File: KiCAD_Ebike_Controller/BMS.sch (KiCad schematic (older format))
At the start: 3 parts

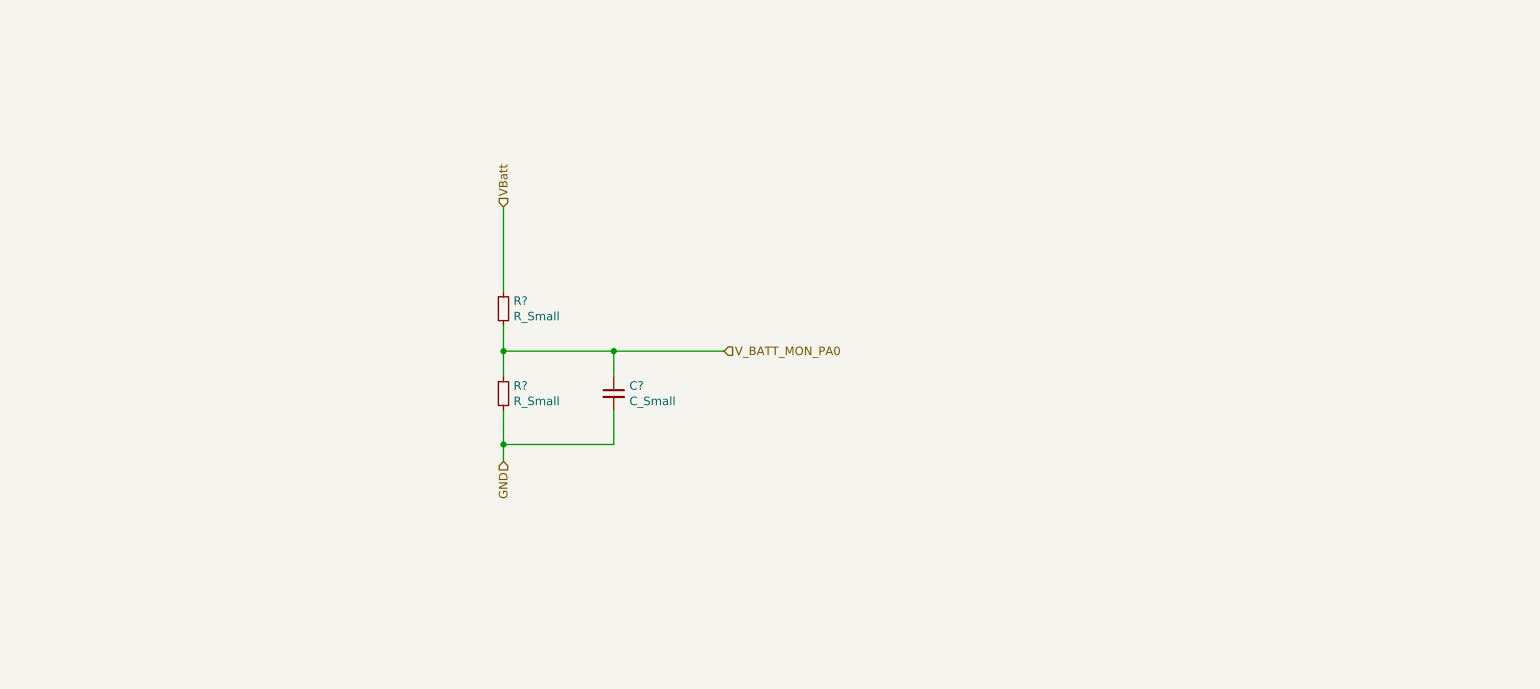
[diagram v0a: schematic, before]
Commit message: close to being done, need to add current pull ups on i2c
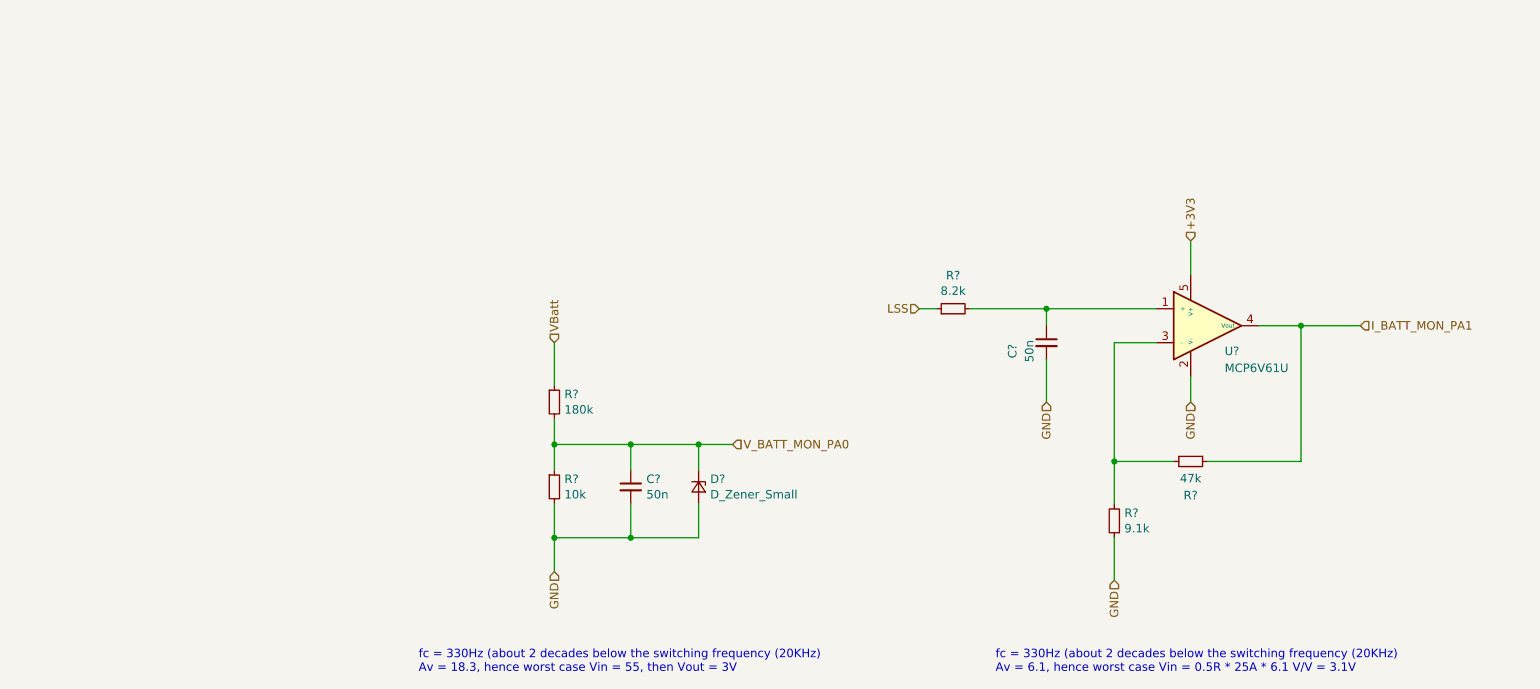
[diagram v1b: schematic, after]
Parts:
- added C?: 50n, symbol Device:C_Small
- added D?: D_Zener_Small, symbol Device:D_Zener_Small
- added R?: 9.1k, symbol Device:R_Small
- added R?: 47k, symbol Device:R_Small
- added R?: 8.2k, symbol Device:R_Small
- added U?: MCP6V61U, symbol Amplifier_Operational:MCP6V61U
- C?: value C_Small -> 50n
- R?: value R_Small -> 180k
- R?: value R_Small -> 10k
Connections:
- net GND: now also C?.2, D?.2 (A), R?.1, U?.2 (V-)
- net V_BATT_MON_PA0: now also D?.1 (K)
- new net: C?.1, R?.2, U?.1 (+)
- new net: R?.2, R?.2, U?.3 (-)
- new net +3V3: U?.5 (V+)
- new net I_BATT_MON_PA1: R?.1, U?.4 (Vout)
- new net LSS: R?.1
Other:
- note added: "fc = 330Hz (about 2 decades below the switching frequency (20KHz)\nAv = 18.3, hence worst case Vin = 55, then Vout = 3V"
- note added: "fc = 330Hz (about 2 decades below the switching frequency (20KHz)\nAv = 6.1, hence worst case Vin = 0.5R * 25A * 6.1 V/V = 3.1V"
- moved on the sheet: C?, R?
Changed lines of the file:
@@
 Comment4 ""
 $EndDescr
-$Comp
-L Device:R_Small R?
-U 1 1 5FA0C8B2
-P 4250 3200
-F 0 "R?" H 4309 3246 50  0000 L CNN
-F 1 "R_Small" H 4309 3155 50  0000 L CNN
-F 2 "" H 4250 3200 50  0001 C CNN
-F 3 "~" H 4250 3200 50  0001 C CNN
-	1    4250 3200
-	1    0    0    -1
-$EndComp
-$Comp
-L Device:R_Small R?
-U 1 1 5FA0CBBA
-P 4250 3700
-F 0 "R?" H 4309 3746 50  0000 L CNN
-F 1 "R_Small" H 4309 3655 50  0000 L CNN
-F 2 "" H 4250 3700 50  0001 C CNN
-F 3 "~" H 4250 3700 50  0001 C CNN
-	1    4250 3700
-	1    0    0    -1
-$EndComp
-Wire Wire Line
-	4250 3300 4250 3450
-Wire Wire Line
-	4250 3800 4250 4000
-Text HLabel 4250 4100 3    50   Input ~ 0
-GND
-Wire Wire Line
-	4250 2600 4250 3100
-Text HLabel 4250 2600 1    50   Input ~ 0
-VBatt
+Text HLabel 5600 4000 2    50   Input ~ 0
+V_BATT_MON_PA0
+Wire Wire Line
+	5000 4000 5400 4000
+Wire Wire Line
+	5000 4000 5000 4150
+Wire Wire Line
+	4550 4000 4550 4150
+Connection ~ 5000 4000
+Wire Wire Line
+	5000 4000 4550 4000
+Wire Wire Line
+	5000 4550 4550 4550
+Wire Wire Line
+	5000 4350 5000 4550
 $Comp
 L Device:C_Small C?
 U 1 1 5FA0D6A7
-P 4900 3700
-F 0 "C?" H 4992 3746 50  0000 L CNN
-F 1 "C_Small" H 4992 3655 50  0000 L CNN
-F 2 "" H 4900 3700 50  0001 C CNN
-F 3 "~" H 4900 3700 50  0001 C CNN
-	1    4900 3700
-	1    0    0    -1
-$EndComp
-Wire Wire Line
-	4900 3800 4900 4000
-Wire Wire Line
-	4900 4000 4250 4000
-Connection ~ 4250 4000
-Wire Wire Line
-	4250 4000 4250 4100
-Wire Wire Line
-	4900 3450 4250 3450
-Connection ~ 4250 3450
-Wire Wire Line
-	4250 3450 4250 3600
-Wire Wire Line
-	4900 3450 4900 3600
-Wire Wire Line
-	4900 3450 5550 3450
-Connection ~ 4900 3450
-Text HLabel 5550 3450 2    50   Input ~ 0
-V_BATT_MON_PA0
+P 5000 4250
+AR Path="/5FA09684/5FA0D6A7" Ref="C?"  Part="1"
+AR Path="/5FA215E4/5FA0D6A7" Ref="C?"  Part="1"
+F 0 "C?" H 5092 4296 50  0000 L CNN
+F 1 "50n" H 5092 4205 50  0000 L CNN
+F 2 "" H 5000 4250 50  0001 C CNN
+F 3 "~" H 5000 4250 50  0001 C CNN
+	1    5000 4250
+	1    0    0    -1
+$EndComp
+Text HLabel 4550 3400 1    50   Input ~ 0
+VBatt
+Wire Wire Line
+	4550 3400 4550 3650
+Text HLabel 7850 4800 3    50   Input ~ 0
+GND
+Connection ~ 4550 4550
+Wire Wire Line
+	4550 4350 4550 4550
+Connection ~ 4550 4000
+Wire Wire Line
+	4550 3850 4550 4000
+$Comp
+L Device:R_Small R?
+U 1 1 5FA0CBBA
+P 4550 4250
+AR Path="/5FA09684/5FA0CBBA" Ref="R?"  Part="1"
+AR Path="/5FA215E4/5FA0CBBA" Ref="R?"  Part="1"
+F 0 "R?" H 4609 4296 50  0000 L CNN
+F 1 "10k" H 4609 4205 50  0000 L CNN
+F 2 "" H 4550 4250 50  0001 C CNN
+F 3 "~" H 4550 4250 50  0001 C CNN
+	1    4550 4250
+	1    0    0    -1
+$EndComp
+$Comp
+L Device:R_Small R?
+U 1 1 5FA0C8B2
+P 4550 3750
+AR Path="/5FA09684/5FA0C8B2" Ref="R?"  Part="1"
+AR Path="/5FA215E4/5FA0C8B2" Ref="R?"  Part="1"
+F 0 "R?" H 4609 3796 50  0000 L CNN
+F 1 "180k" H 4609 3705 50  0000 L CNN
+F 2 "" H 4550 3750 50  0001 C CNN
+F 3 "~" H 4550 3750 50  0001 C CNN
+	1    4550 3750
+	1    0    0    -1
+$EndComp
+Text HLabel 6700 3200 0    50   Input ~ 0
+LSS
+Text HLabel 8300 2800 1    50   Input ~ 0
++3V3
+Text HLabel 9300 3300 2    50   Input ~ 0
+I_BATT_MON_PA1
+Wire Wire Line
+	4550 4550 4550 4750
+Text Notes 7150 5350 0    50   ~ 0
+fc = 330Hz (about 2 decades below the switching frequency (20KHz)\nAv = 6.1, hence worst case Vin = 0.5R * 25A * 6.1 V/V = 3.1V
+Wire Wire Line
+	7850 3400 8100 3400
+$Comp
+L Amplifier_Operational:MCP6V61U U?
+U 1 1 5F9A8CBA
+P 8100 3200
+AR Path="/5FA09684/5F9A8CBA" Ref="U?"  Part="1"
+AR Path="/5FA215E4/5F9A8CBA" Ref="U?"  Part="1"
+F 0 "U?" H 8500 2950 50  0000 L CNN
+F 1 "MCP6V61U" H 8500 2850 50  0000 L CNN
+F 2 "" H 8000 2450 50  0001 C CNN
+F 3 "" H 8000 2450 50  0001 C CNN
+	1    8100 3200
+	1    0    0    -1
+$EndComp
+Wire Wire Line
+	8700 3300 8950 3300
+$Comp
+L Device:C_Small C?
+U 1 1 5F9EC77C
+P 7450 3400
+AR Path="/5FA09684/5F9EC77C" Ref="C?"  Part="1"
+AR Path="/5FA215E4/5F9EC77C" Ref="C?"  Part="1"
+F 0 "C?" V 7650 3350 50  0000 C CNN
+F 1 "50n" V 7550 3350 50  0000 C CNN
+F 2 "" H 7450 3400 50  0001 C CNN
+F 3 "~" H 7450 3400 50  0001 C CNN
+	1    7450 3400
+	-1   0    0    -1
+$EndComp
+$Comp
+L Device:R_Small R?
+U 1 1 5F9EFB76
+P 7850 4450
+AR Path="/5FA09684/5F9EFB76" Ref="R?"  Part="1"
+AR Path="/5FA215E4/5F9EFB76" Ref="R?"  Part="1"
+F 0 "R?" H 7791 4404 50  0000 R CNN
+F 1 "9.1k" H 7791 4495 50  0000 R CNN
+F 2 "" H 7850 4450 50  0001 C CNN
+F 3 "~" H 7850 4450 50  0001 C CNN
+	1    7850 4450
+	-1   0    0    1
+$EndComp
+$Comp
+L Device:R_Small R?
+U 1 1 5F9F022F
+P 8300 4100
+AR Path="/5FA09684/5F9F022F" Ref="R?"  Part="1"
+AR Path="/5FA215E4/5F9F022F" Ref="R?"  Part="1"
+F 0 "R?" V 8500 4100 50  0000 C CNN
+F 1 "47k" V 8400 4100 50  0000 C CNN
+F 2 "" H 8300 4100 50  0001 C CNN
+F 3 "~" H 8300 4100 50  0001 C CNN
+	1    8300 4100
+	0    1    1    0
+$EndComp
+Wire Wire Line
+	6700 3200 6800 3200
+$Comp
+L Device:R_Small R?
+U 1 1 5F9FB5C2
+P 6900 3200
+AR Path="/5FA09684/5F9FB5C2" Ref="R?"  Part="1"
+AR Path="/5FA215E4/5F9FB5C2" Ref="R?"  Part="1"
+F 0 "R?" V 7096 3200 50  0000 C CNN
+F 1 "8.2k" V 7005 3200 50  0000 C CNN
+F 2 "" H 6900 3200 50  0001 C CNN
+F 3 "~" H 6900 3200 50  0001 C CNN
+	1    6900 3200
+	0    -1   -1   0
+$EndComp
+Wire Wire Line
+	7000 3200 7450 3200
+Wire Wire Line
+	7450 3300 7450 3200
+Connection ~ 7450 3200
+Wire Wire Line
+	7450 3200 8100 3200
+Wire Wire Line
+	8400 4100 8950 4100
+Wire Wire Line
+	8950 4100 8950 3300
+Connection ~ 8950 3300
+Wire Wire Line
+	8950 3300 9300 3300
+Wire Wire Line
+	8200 4100 7850 4100
+Wire Wire Line
+	7850 4100 7850 3400
+Wire Wire Line
+	7850 4100 7850 4350
+Connection ~ 7850 4100
+Wire Wire Line
+	7850 4800 7850 4550
+Text Notes 3750 5350 0    50   ~ 0
+fc = 330Hz (about 2 decades below the switching frequency (20KHz)\nAv = 18.3, hence worst case Vin = 55, then Vout = 3V
+Wire Wire Line
+	8300 2800 8300 3000
+Text HLabel 8300 3750 3    50   Input ~ 0
+GND
+Text HLabel 7450 3750 3    50   Input ~ 0
+GND
+Wire Wire Line
+	7450 3500 7450 3750
+Wire Wire Line
+	8300 3600 8300 3750
+Text HLabel 4550 4750 3    50   Input ~ 0
+GND
+$Comp
+L Device:D_Zener_Small D?
+U 1 1 5FA37BFA
+P 5400 4250
+F 0 "D?" V 5354 4318 50  0000 L CNN
+F 1 "D_Zener_Small" V 5445 4318 50  0000 L CNN
+F 2 "" V 5400 4250 50  0001 C CNN
+F 3 "~" V 5400 4250 50  0001 C CNN
+	1    5400 4250
+	0    1    1    0
+$EndComp
+Wire Wire Line
+	5400 4150 5400 4000
+Connection ~ 5400 4000
+Wire Wire Line
+	5400 4000 5600 4000
+Wire Wire Line
+	5400 4350 5400 4550
+Wire Wire Line
+	5400 4550 5000 4550
+Connection ~ 5000 4550
 $EndSCHEMATC

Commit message: schem done
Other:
- note added: "fc = 330Hz (about 2 decades below the switching frequency (20KHz)\nAv = 18.3, hence worst case Vin = 55, then Vout = 3V\nEquivilent resistance is 9.5K, so no need for buffer amp"
- note removed: "fc = 330Hz (about 2 decades below the switching frequency (20KHz)\nAv = 18.3, hence worst case Vin = 55, then Vout = 3V"
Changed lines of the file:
@@
 	7850 4800 7850 4550
 Text Notes 3750 5350 0    50   ~ 0
-fc = 330Hz (about 2 decades below the switching frequency (20KHz)\nAv = 18.3, hence worst case Vin = 55, then Vout = 3V
+fc = 330Hz (about 2 decades below the switching frequency (20KHz)\nAv = 18.3, hence worst case Vin = 55, then Vout = 3V\nEquivilent resistance is 9.5K, so no need for buffer amp
 Wire Wire Line
 	8300 2800 8300 3000

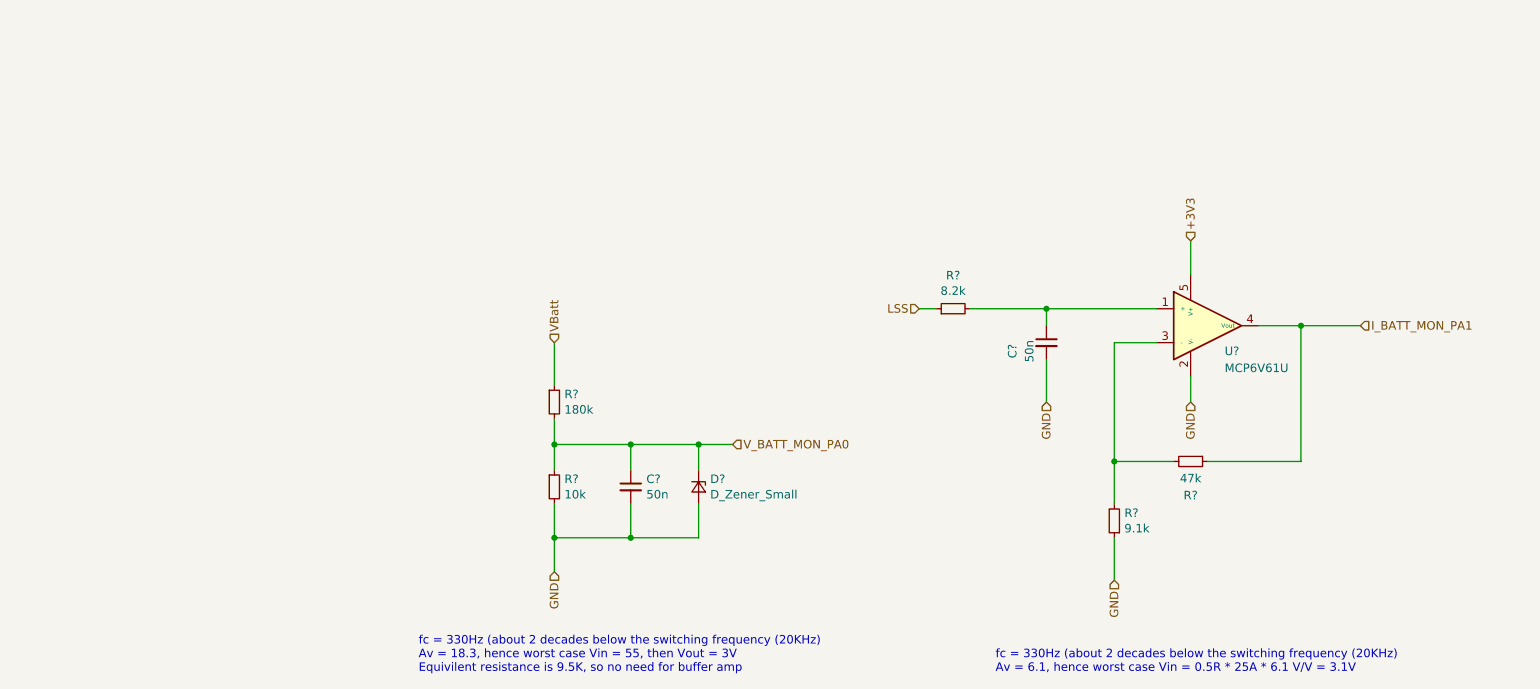
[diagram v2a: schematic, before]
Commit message: adding footprints
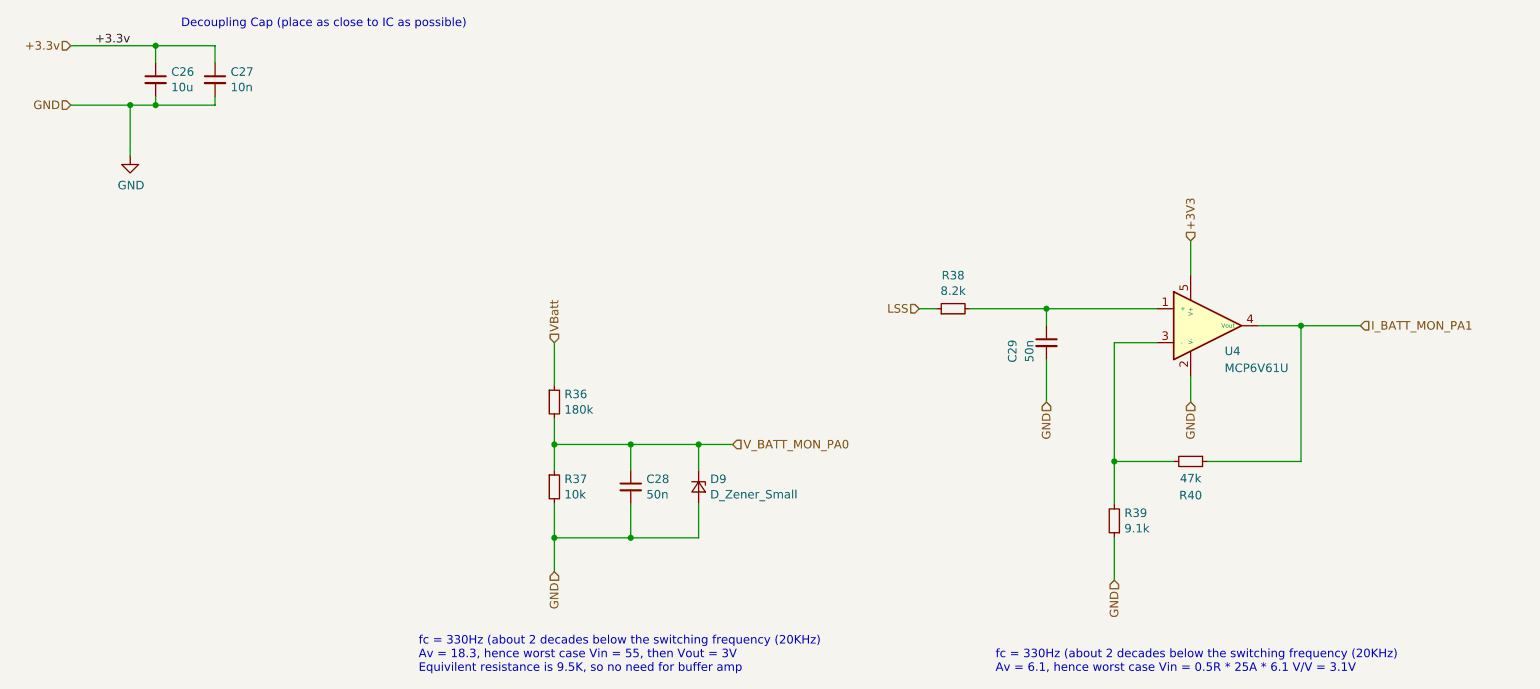
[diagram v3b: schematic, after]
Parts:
- added C26: 10u, Capacitor_SMD:C_0805_2012Metric, symbol Device:C_Small
- added C27: 10n, Capacitor_SMD:C_0805_2012Metric, symbol Device:C_Small
- C28, C29: renamed from C?; footprint (none) -> Capacitor_SMD:C_0805_2012Metric_Pad1.15x1.40mm_HandSolder
- gave numbers to parts that had none: 7
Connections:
- net GND: now also C26.2, C27.2
- new net +3.3v: C26.1, C27.1
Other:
- note added: "Decoupling Cap (place as close to IC as possible)"
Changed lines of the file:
@@
 $Descr A4 11693 8268
 encoding utf-8
-Sheet 7 7
+Sheet 6 7
 Title ""
 Date ""
@@
 P 5000 4250
 AR Path="/5FA09684/5FA0D6A7" Ref="C?"  Part="1"
-AR Path="/5FA215E4/5FA0D6A7" Ref="C?"  Part="1"
-F 0 "C?" H 5092 4296 50  0000 L CNN
+AR Path="/5FA215E4/5FA0D6A7" Ref="C28"  Part="1"
+F 0 "C28" H 5092 4296 50  0000 L CNN
 F 1 "50n" H 5092 4205 50  0000 L CNN
-F 2 "" H 5000 4250 50  0001 C CNN
+F 2 "Capacitor_SMD:C_0805_2012Metric_Pad1.15x1.40mm_HandSolder" H 5000 4250 50  0001 C CNN
 F 3 "~" H 5000 4250 50  0001 C CNN
 	1    5000 4250
@@
 P 4550 4250
 AR Path="/5FA09684/5FA0CBBA" Ref="R?"  Part="1"
-AR Path="/5FA215E4/5FA0CBBA" Ref="R?"  Part="1"
-F 0 "R?" H 4609 4296 50  0000 L CNN
+AR Path="/5FA215E4/5FA0CBBA" Ref="R37"  Part="1"
+F 0 "R37" H 4609 4296 50  0000 L CNN
 F 1 "10k" H 4609 4205 50  0000 L CNN
 F 2 "" H 4550 4250 50  0001 C CNN
@@
 P 4550 3750
 AR Path="/5FA09684/5FA0C8B2" Ref="R?"  Part="1"
-AR Path="/5FA215E4/5FA0C8B2" Ref="R?"  Part="1"
-F 0 "R?" H 4609 3796 50  0000 L CNN
+AR Path="/5FA215E4/5FA0C8B2" Ref="R36"  Part="1"
+F 0 "R36" H 4609 3796 50  0000 L CNN
 F 1 "180k" H 4609 3705 50  0000 L CNN
 F 2 "" H 4550 3750 50  0001 C CNN
@@
 P 8100 3200
 AR Path="/5FA09684/5F9A8CBA" Ref="U?"  Part="1"
-AR Path="/5FA215E4/5F9A8CBA" Ref="U?"  Part="1"
-F 0 "U?" H 8500 2950 50  0000 L CNN
+AR Path="/5FA215E4/5F9A8CBA" Ref="U4"  Part="1"
+F 0 "U4" H 8500 2950 50  0000 L CNN
 F 1 "MCP6V61U" H 8500 2850 50  0000 L CNN
 F 2 "" H 8000 2450 50  0001 C CNN
@@
 P 7450 3400
 AR Path="/5FA09684/5F9EC77C" Ref="C?"  Part="1"
-AR Path="/5FA215E4/5F9EC77C" Ref="C?"  Part="1"
-F 0 "C?" V 7650 3350 50  0000 C CNN
+AR Path="/5FA215E4/5F9EC77C" Ref="C29"  Part="1"
+F 0 "C29" V 7650 3350 50  0000 C CNN
 F 1 "50n" V 7550 3350 50  0000 C CNN
-F 2 "" H 7450 3400 50  0001 C CNN
+F 2 "Capacitor_SMD:C_0805_2012Metric_Pad1.15x1.40mm_HandSolder" H 7450 3400 50  0001 C CNN
 F 3 "~" H 7450 3400 50  0001 C CNN
 	1    7450 3400
@@
 P 7850 4450
 AR Path="/5FA09684/5F9EFB76" Ref="R?"  Part="1"
-AR Path="/5FA215E4/5F9EFB76" Ref="R?"  Part="1"
-F 0 "R?" H 7791 4404 50  0000 R CNN
+AR Path="/5FA215E4/5F9EFB76" Ref="R39"  Part="1"
+F 0 "R39" H 7791 4404 50  0000 R CNN
 F 1 "9.1k" H 7791 4495 50  0000 R CNN
 F 2 "" H 7850 4450 50  0001 C CNN
@@
 P 8300 4100
 AR Path="/5FA09684/5F9F022F" Ref="R?"  Part="1"
-AR Path="/5FA215E4/5F9F022F" Ref="R?"  Part="1"
-F 0 "R?" V 8500 4100 50  0000 C CNN
+AR Path="/5FA215E4/5F9F022F" Ref="R40"  Part="1"
+F 0 "R40" V 8500 4100 50  0000 C CNN
 F 1 "47k" V 8400 4100 50  0000 C CNN
 F 2 "" H 8300 4100 50  0001 C CNN
@@
 P 6900 3200
 AR Path="/5FA09684/5F9FB5C2" Ref="R?"  Part="1"
-AR Path="/5FA215E4/5F9FB5C2" Ref="R?"  Part="1"
-F 0 "R?" V 7096 3200 50  0000 C CNN
+AR Path="/5FA215E4/5F9FB5C2" Ref="R38"  Part="1"
+F 0 "R38" V 7096 3200 50  0000 C CNN
 F 1 "8.2k" V 7005 3200 50  0000 C CNN
 F 2 "" H 6900 3200 50  0001 C CNN
@@
 GND
 $Comp
-L Device:D_Zener_Small D?
+L Device:D_Zener_Small D9
 U 1 1 5FA37BFA
 P 5400 4250
-F 0 "D?" V 5354 4318 50  0000 L CNN
+F 0 "D9" V 5354 4318 50  0000 L CNN
 F 1 "D_Zener_Small" V 5445 4318 50  0000 L CNN
 F 2 "" V 5400 4250 50  0001 C CNN
@@
 	5400 4550 5000 4550
 Connection ~ 5000 4550
+Text HLabel 1700 2000 0    50   Input ~ 0
+GND
+$Comp
+L power:GND #PWR?
+U 1 1 5FCA94F0
+P 2050 2300
+AR Path="/5F8BD648/5FCA94F0" Ref="#PWR?"  Part="1"
+AR Path="/5FA215E4/5FCA94F0" Ref="#PWR0128"  Part="1"
+F 0 "#PWR0128" H 2050 2050 50  0001 C CNN
+F 1 "GND" H 2055 2127 50  0000 C CNN
+F 2 "" H 2050 2300 50  0001 C CNN
+F 3 "" H 2050 2300 50  0001 C CNN
+	1    2050 2300
+	1    0    0    -1
+$EndComp
+Wire Wire Line
+	1700 2000 2050 2000
+Wire Wire Line
+	2050 2000 2050 2300
+Text Label 2050 1650 2    50   ~ 0
++3.3v
+$Comp
+L Device:C_Small C?
+U 1 1 5FCA94F9
+P 2200 1850
+AR Path="/5F8BD648/5FCA94F9" Ref="C?"  Part="1"
+AR Path="/5FA215E4/5FCA94F9" Ref="C26"  Part="1"
+F 0 "C26" H 2292 1896 50  0000 L CNN
+F 1 "10u" H 2292 1805 50  0000 L CNN
+F 2 "Capacitor_SMD:C_0805_2012Metric" H 2200 1850 50  0001 C CNN
+F 3 "~" H 2200 1850 50  0001 C CNN
+	1    2200 1850
+	1    0    0    -1
+$EndComp
+Wire Wire Line
+	2200 1950 2200 2000
+Wire Wire Line
+	2200 2000 2050 2000
+Connection ~ 2050 2000
+Wire Wire Line
+	2200 1750 2200 1650
+Wire Wire Line
+	1700 1650 2200 1650
+Text Notes 2350 1550 0    50   ~ 0
+Decoupling Cap (place as close to IC as possible)
+$Comp
+L Device:C_Small C?
+U 1 1 5FCA9505
+P 2550 1850
+AR Path="/5F8BD648/5FCA9505" Ref="C?"  Part="1"
+AR Path="/5FA215E4/5FCA9505" Ref="C27"  Part="1"
+F 0 "C27" H 2642 1896 50  0000 L CNN
+F 1 "10n" H 2642 1805 50  0000 L CNN
+F 2 "Capacitor_SMD:C_0805_2012Metric" H 2550 1850 50  0001 C CNN
+F 3 "~" H 2550 1850 50  0001 C CNN
+	1    2550 1850
+	1    0    0    -1
+$EndComp
+Wire Wire Line
+	2550 1750 2550 1650
+Wire Wire Line
+	2550 1650 2200 1650
+Connection ~ 2200 1650
+Wire Wire Line
+	2550 1950 2550 2000
+Wire Wire Line
+	2550 2000 2200 2000
+Connection ~ 2200 2000
+Text HLabel 1700 1650 0    50   Input ~ 0
++3.3v
 $EndSCHEMATC
